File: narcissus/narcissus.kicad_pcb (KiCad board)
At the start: 2 copper layers, 115 x 148 mm, 72 parts, among them J1 NEIGHBOR1, J2 NEIGHBOR2, U1 PCA9698, U2 PCA9698, U3 AP2553W6-7, U4 74HC4051

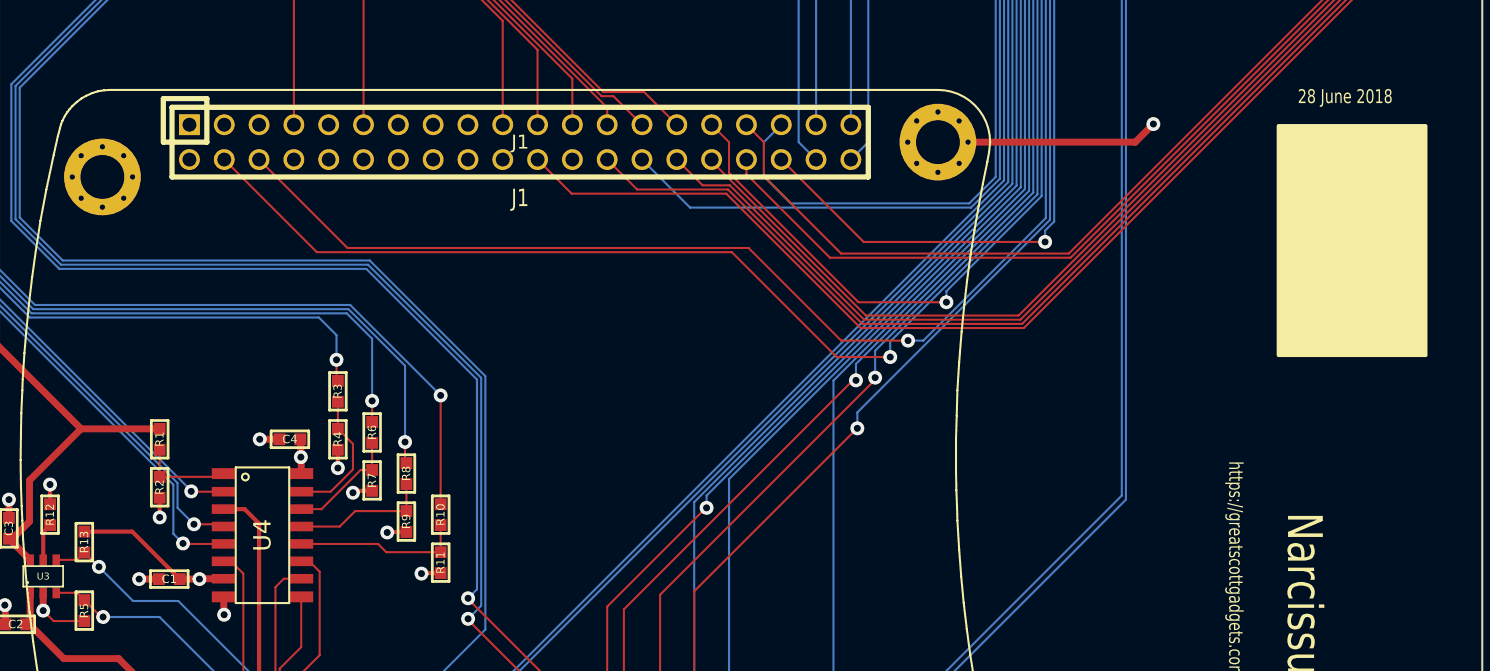
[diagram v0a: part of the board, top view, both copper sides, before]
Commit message: Narcissus: corrected U4 pin 7 power supply connection
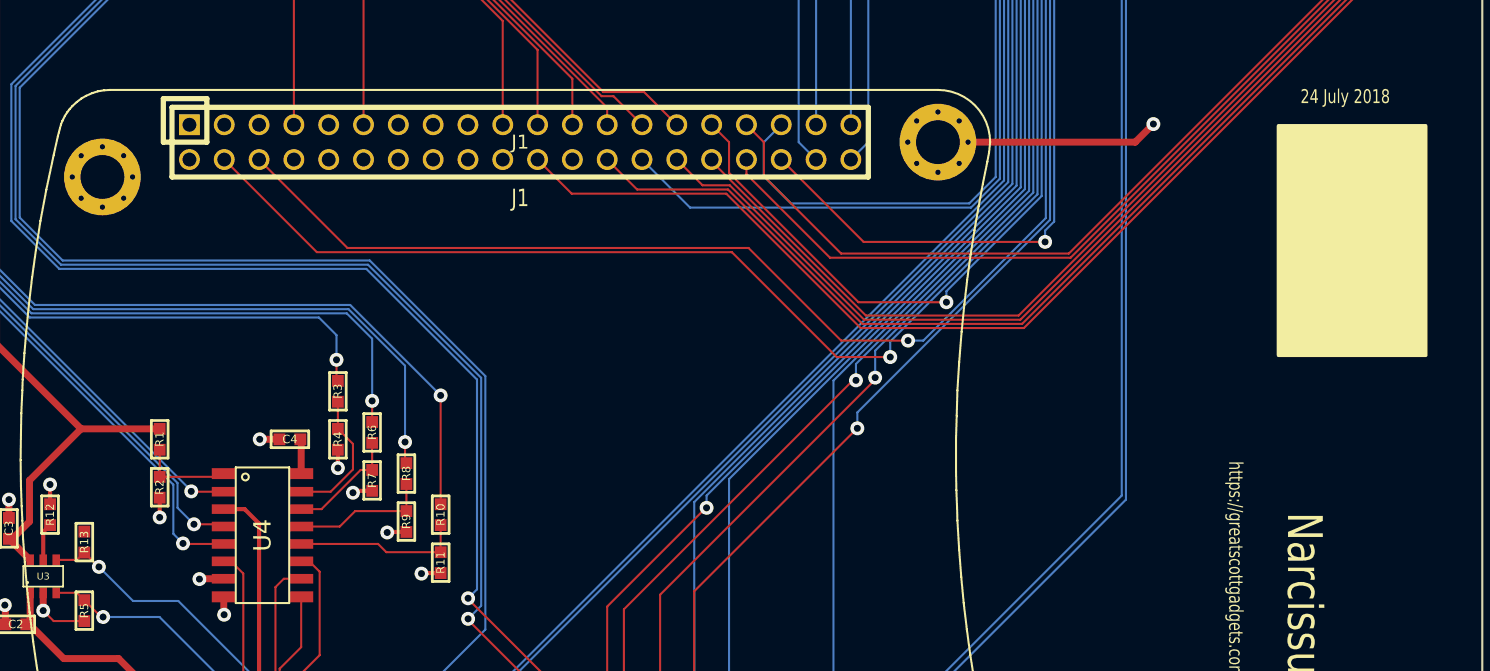
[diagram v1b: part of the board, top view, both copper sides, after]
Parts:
- removed C1: 100nF, gsg-modules:0603
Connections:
- J1 pad 10: (no net) -> /P1_1
- J1 pad 12: (no net) -> /P1_2
- J1 pad 13: (no net) -> /P1_5
- J1 pad 14: (no net) -> /P5_2
- J1 pad 15: (no net) -> /P1_7
- J1 pad 16: (no net) -> /P1_6
- J1 pad 17: (no net) -> /P1_9
- J1 pad 18: (no net) -> /P1_8
- J1 pad 20: (no net) -> /P1_10
- J1 pad 24: (no net) -> /P5_4
- J1 pad 3: (no net) -> /P4_9
- J1 pad 5: (no net) -> /P4_10
- J1 pad 8: (no net) -> /P5_0
- J1 pad 9: (no net) -> /P5_1
- J2 pad 12: (no net) -> /CLK2
- J2 pad 13: (no net) -> /P2_8
- J2 pad 14: (no net) -> /P2_7
- J2 pad 15: (no net) -> /P2_6
- J2 pad 16: (no net) -> /P7_7
- J2 pad 17: (no net) -> /WAKEUP0
- J2 pad 18: (no net) -> /P2_5
- J2 pad 27: (no net) -> /P7_0
- J2 pad 28: (no net) -> /P3_4
- J2 pad 29: (no net) -> /P6_8
- J2 pad 31: (no net) -> /P6_7
- J2 pad 33: (no net) -> /P2_2
- J2 pad 34: (no net) -> /P6_6
- J2 pad 35: (no net) -> /P2_1
- J2 pad 36: (no net) -> /P6_3
- J2 pad 37: (no net) -> /P3_5
- J2 pad 9: (no net) -> /P4_3
- U4 pad 7: VCC -> GND
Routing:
- net VCC: track 137.6 -> 126.1 mm, vias 12 -> 10
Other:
- board text added: "24 July 2018"
- board text removed: "28 June 2018"
